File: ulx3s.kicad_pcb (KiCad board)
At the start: 4 copper layers, 94 x 50.8 mm, 121 parts, among them J1 CONN_02X20, J2 CONN_02X20, J4 CONN_02X03, J6 WIFI_OFF, U1 LFE5U-85F-6BG381C, U10 IS25LP128F-JBLE, U2 IS42S16160J-6TL, U3 TLV62569DBV, U4 TLV62569DBV, U5 TLV62569DBV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

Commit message: remove buttons f1/f2
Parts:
- removed B1, B2: PTS645, Button_Switch_SMD:SW_SPST_PTS645
- removed R7: 130, Resistor_SMD:R_0603_1608Metric
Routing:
- net /blinkey/BTNPUL: track 45.6 -> 0.00 mm, vias 1 -> 0
- net BTN_F1: track 41.4 -> 0.00 mm, vias 2 -> 0
- net BTN_F2: track 28.0 -> 14.4 mm
- net +3V3: track 258.1 -> 256.4 mm

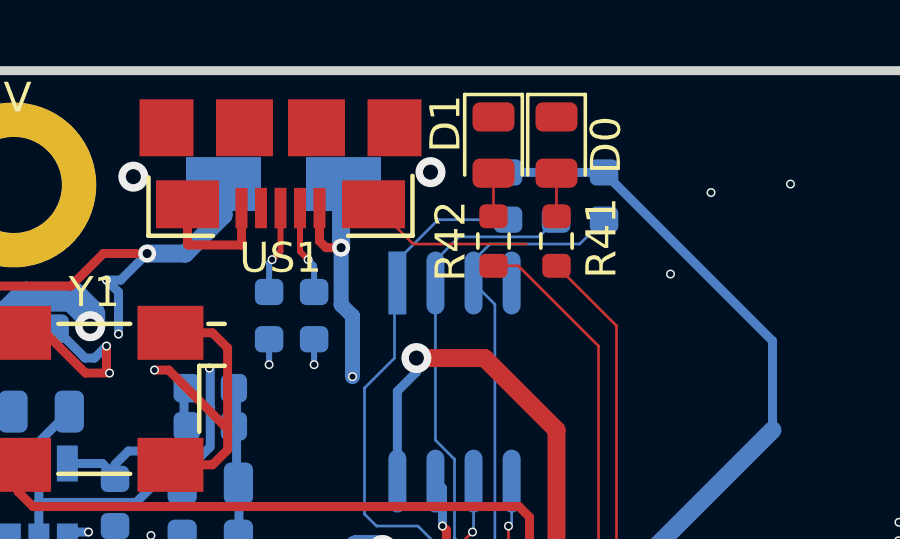
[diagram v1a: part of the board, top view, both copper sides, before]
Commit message: remove hanging track
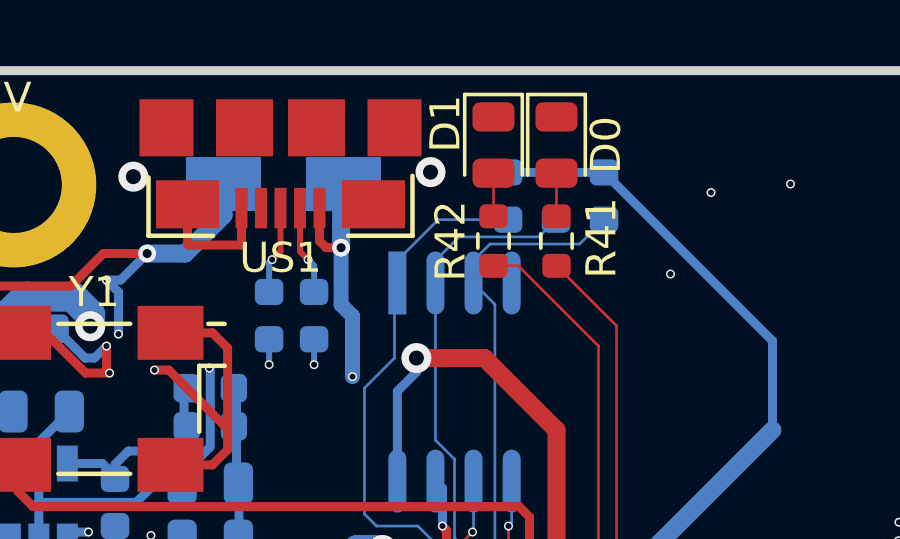
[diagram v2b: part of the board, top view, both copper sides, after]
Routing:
- net GND: track 350.0 -> 344.4 mm
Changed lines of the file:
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@@
-	)
-	(segment
-		(start 116.305 67.2)
-		(end 120.08 67.2)
-		(width 0.09)
-		(layer "F.Cu")
-		(net "GND")
 	)
 	(segment
@@
 		(layer "F.Cu")
 		(net "GND")
-	)
-	(segment
-		(start 114.98 65.875)
-		(end 116.305 67.2)
-		(width 0.09)
-		(layer "F.Cu")
-		(net "GND")

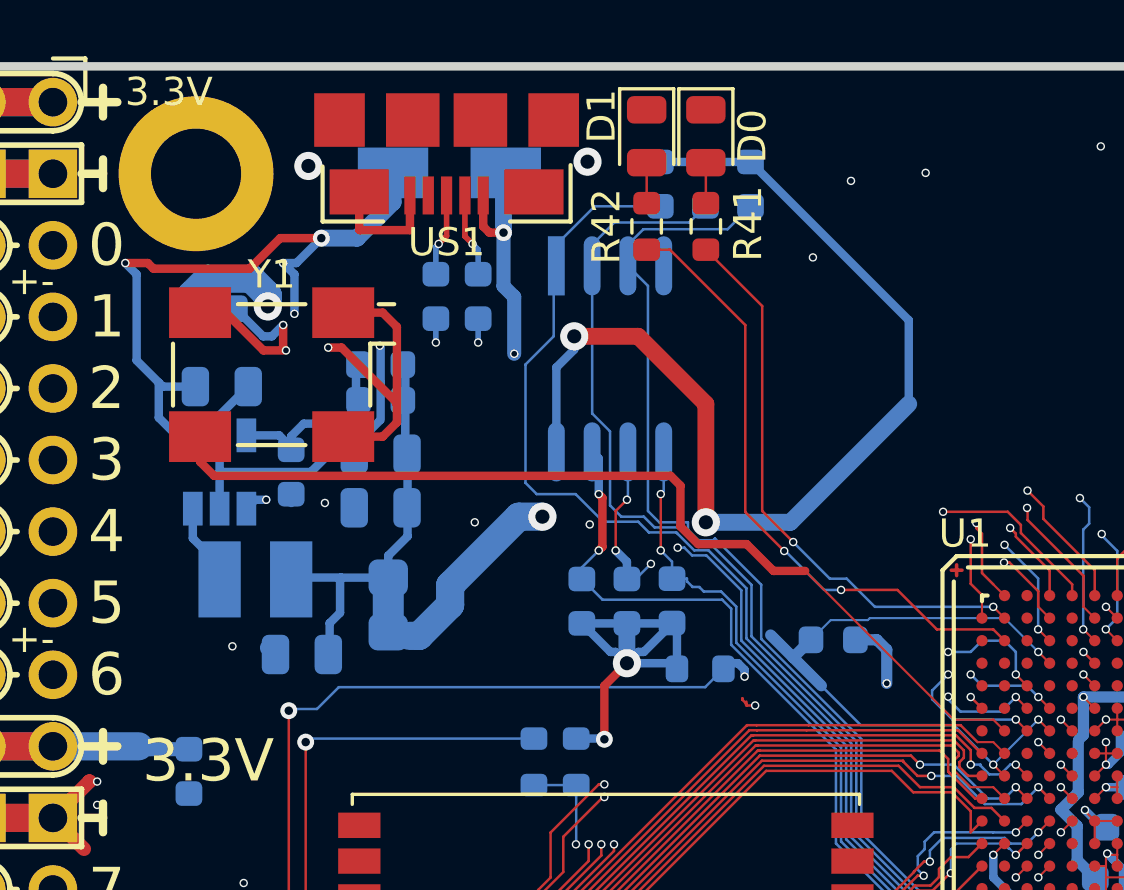
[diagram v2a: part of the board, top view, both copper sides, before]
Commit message: reposition clock to top of board
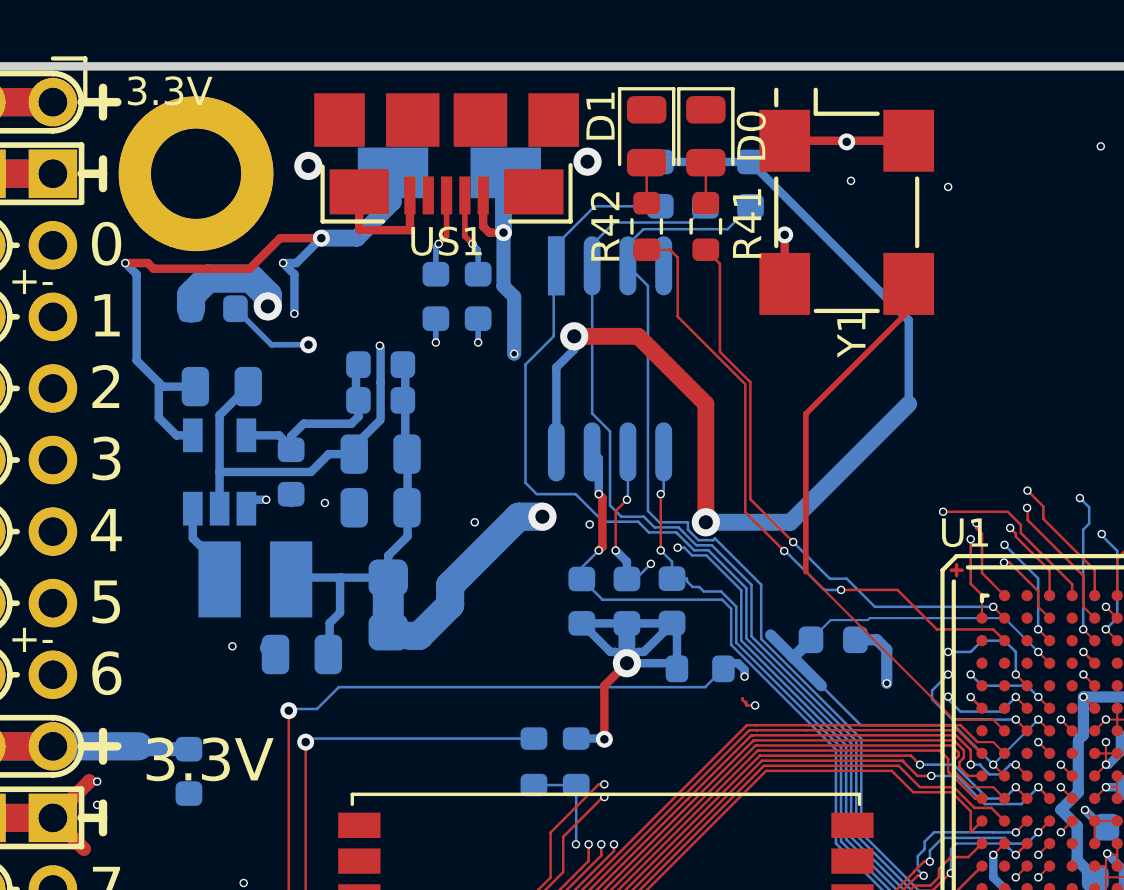
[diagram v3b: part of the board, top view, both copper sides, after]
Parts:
- moved Y1 21.2 mm to (126.1, 66.6), turned to -90 degrees
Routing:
- net CLK_25MHz: track 34.2 -> 20.2 mm
- net +3V3: track 256.4 -> 249.9 mm
- net GND: track 344.4 -> 343.4 mm, vias 125 -> 124
